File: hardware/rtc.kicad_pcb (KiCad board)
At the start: 2 copper layers, 45 x 35 mm, 39 parts, among them J1 AKL_5_2, J2 AKL_5_2, J3 DB9, P1 CON-SENSOR, SW1 Termination, U1 M24C64, U2 MCP2515, U3 MCP2562, U4 DRILL, U5 DRILL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

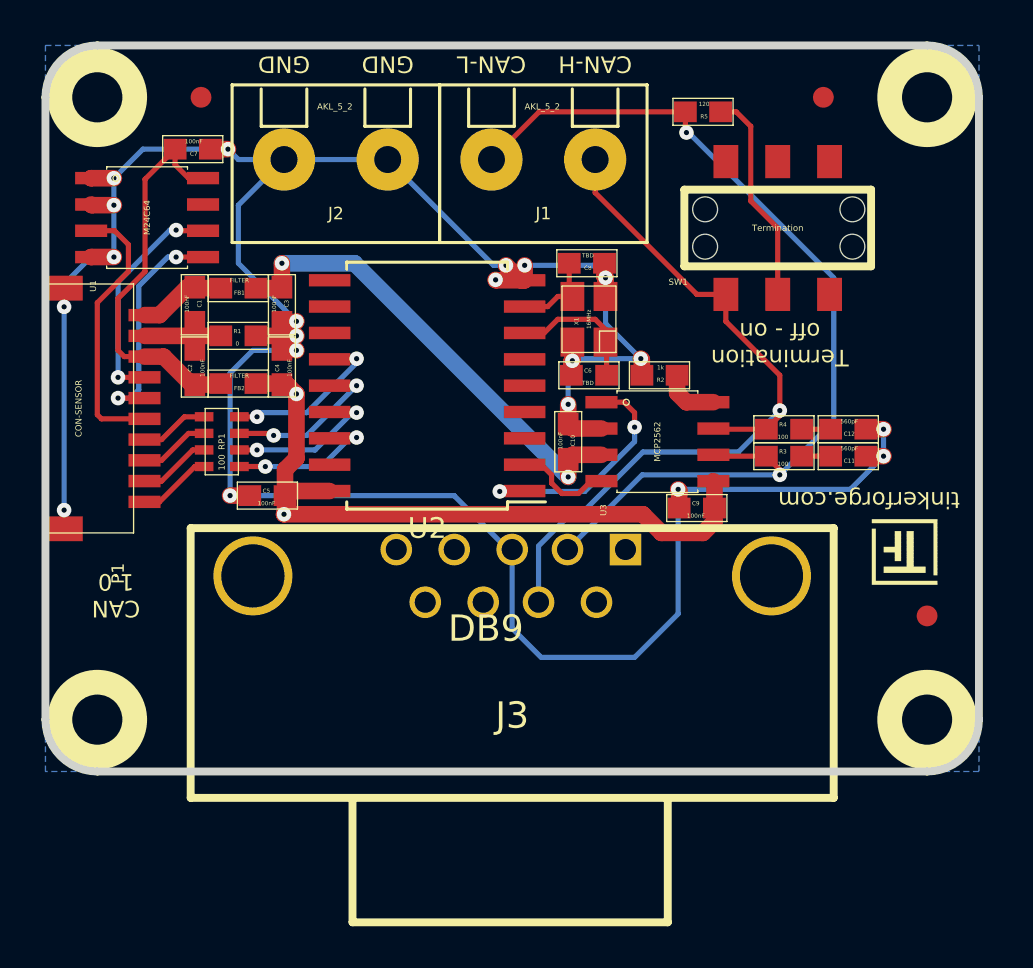
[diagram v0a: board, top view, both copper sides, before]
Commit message: fully routed
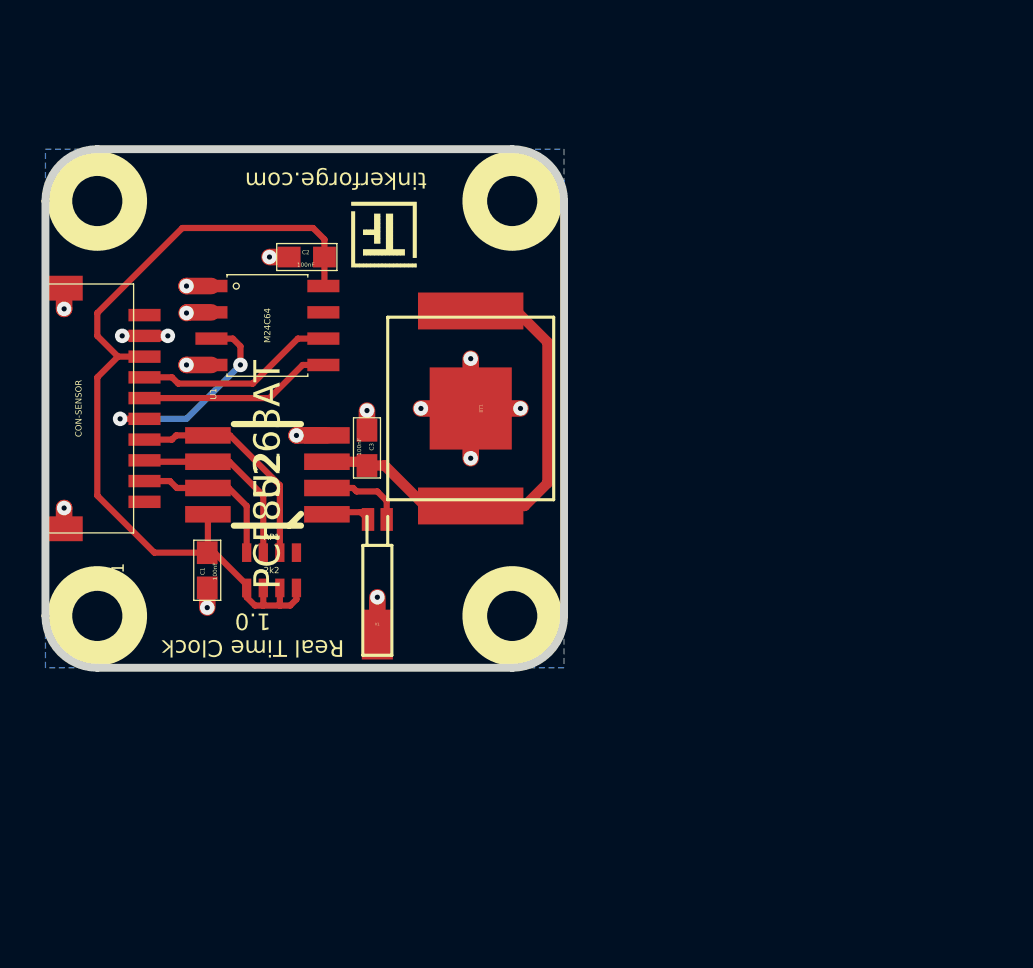
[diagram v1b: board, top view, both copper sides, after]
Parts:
- removed C10, C4, C5, C7, C9: 100nF, kicad-libraries:0603E
- removed C11, C12: 560pF, kicad-libraries:0603E
- removed C6, C8: TBD, kicad-libraries:0603E
- removed FB1, FB2: FILTER, kicad-libraries:0603E
- removed Fiducial_Mark (x3): VAL**, Fiducial_Mark
- removed the G*** at (168.3, 109.1)
- removed J1, J2: AKL_5_2, kicad-libraries:AKL_5_2
- removed J3: DB9, kicad-libraries:SUB09-EU
- removed R1: 0, kicad-libraries:0603E
- removed R2: 1k, kicad-libraries:0603E
- removed R3, R4: 100, kicad-libraries:0603E
- removed R5: 120, kicad-libraries:0603E
- removed SW1: Termination, kicad-libraries:SLIDE_SWITCH
- removed U7: DRILL, kicad-libraries:DRILL_NP
- removed the VAL at (143.3, 100.6)
- removed the VAL at (150.3, 100.6)
- added BT1: BATTERY, kicad-libraries:BATTERY_HOLDER_2998, F.Cu at (145.8, 100.6)
- added G***: Logo_31x31, kicad-libraries:Logo_31x31, F.Cu at (143.2, 93.8)
- added VAL: WEEE_7mm_back, kicad-libraries:WEEE_7mm_back, B.Cu at (132.8, 100.6)
- added VAL: CE_5mm, kicad-libraries:CE_5mm, B.Cu at (143.3, 100.6)
- RP1: value 100 -> 2k2; footprint kicad-libraries:0603X4 -> kicad-libraries:4X0603
- U2: value MCP2515 -> PCF85263AT; footprint kicad-libraries:SOIC-18 -> kicad-libraries:SO-8
- U3: value MCP2562 -> DRILL; footprint kicad-libraries:SOIC8 -> kicad-libraries:DRILL_NP
- X1: value 16MHz -> 32.768kHz; footprint kicad-libraries:CRYSTAL_3225 -> kicad-libraries:AB26TRQ
- moved U3 29.4 mm to (127.8, 90.6)
- moved U4 20.6 mm to (147.8, 110.6)
- moved U5 20.6 mm to (147.8, 90.6)
- moved X1 18.3 mm to (141.3, 111.5), turned to 180 degrees
- moved C1 12.8 mm to (133.1, 108.4), turned to 270 degrees
- moved U2 8.82 mm to (136.0, 103.8), turned to 90 degrees
- moved C3 8.03 mm to (140.8, 102.5)
- moved U1 7.79 mm to (136.0, 96.6)
- moved C2 7.57 mm to (137.9, 93.3), turned to 180 degrees
- moved RP1 6.65 mm to (136.2, 108.4), turned to 0 degrees
- moved U6 5.00 mm to (127.8, 110.6)
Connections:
- C1 pad 1: Net-(C1-Pad1) -> 3V3
- C1 pad 2: Net-(C1-Pad2) -> GND
- C2 pad 1: Net-(C1-Pad1) -> 3V3
- C2 pad 2: 3V3 -> GND
- C3 pad 1: GND -> Net-(BT1-Pad1)
- C3 pad 2: +5V -> GND
- P1 pad 1: Net-(C1-Pad2) -> (no net)
- P1 pad 10: Net-(P1-Pad10) -> (no net)
- P1 pad 2: Net-(C1-Pad1) -> GND
- RP1 pad 1: Net-(RP1-Pad1) -> Net-(P1-Pad9)
- RP1 pad 2: Net-(RP1-Pad2) -> Net-(P1-Pad8)
- RP1 pad 3: Net-(RP1-Pad3) -> Net-(P1-Pad7)
- RP1 pad 4: Net-(RP1-Pad4) -> (no net)
- RP1 pad 5: Net-(P1-Pad7) -> 3V3
- RP1 pad 6: Net-(P1-Pad8) -> 3V3
- RP1 pad 7: Net-(P1-Pad9) -> 3V3
- RP1 pad 8: Net-(P1-Pad10) -> 3V3
- U2 pad 3: (no net) -> Net-(BT1-Pad1)
- U2 pad 4: (no net) -> GND
- U2 pad 5: (no net) -> Net-(P1-Pad7)
- U2 pad 6: (no net) -> Net-(P1-Pad8)
- U2 pad 7: Net-(C6-Pad1) -> Net-(P1-Pad9)
- U2 pad 8: Net-(C8-Pad1) -> 3V3
- X1 pad 1: Net-(C6-Pad1) -> Net-(U2-Pad2)
- X1 pad 2: Net-(C8-Pad1) -> Net-(U2-Pad1)
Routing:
- net GND: track 143.4 -> 23.5 mm, vias 20 -> 16
- net Net-(J1-Pad1): track 47.4 -> 0.00 mm, vias 2 -> 0
- net Net-(J1-Pad2): track 37.4 -> 0.00 mm, vias 1 -> 0
- net VCC: track 33.8 -> 0.00 mm, vias 2 -> 0
- net 3V3: track 18.9 -> 42.6 mm
- net Net-(BT1-Pad1): track 0.00 -> 23.1 mm
- net +5V: track 23.0 -> 0.00 mm, vias 2 -> 0
- net Net-(R5-Pad2): track 10.4 -> 0.00 mm
- net Net-(U2-Pad1): track 11.9 -> 2.17 mm, vias 2 -> 0
- net Net-(RP1-Pad4): track 8.44 -> 0.00 mm, vias 2 -> 0
- net Net-(RP1-Pad3): track 7.98 -> 0.00 mm, vias 2 -> 0
- net Net-(RP1-Pad2): track 7.71 -> 0.00 mm, vias 2 -> 0
- net Net-(RP1-Pad1): track 7.55 -> 0.00 mm, vias 2 -> 0
- net Net-(P1-Pad7): track 3.33 -> 10.9 mm
- net Net-(C6-Pad1): track 6.60 -> 0.00 mm
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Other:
- board size 45 x 35 mm -> 25 x 25 mm
- board text added: "Real Time Clock 1.0"
- board text removed: "CAN 1.0"
- board text removed: "CAN-H"
- board text removed: "CAN-L"
- board text removed: "GND"
- board text removed: "Termination off - on"
